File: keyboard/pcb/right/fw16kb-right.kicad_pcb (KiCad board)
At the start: 2 copper layers, 0 parts

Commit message: keyboard right PCB: outline + 2-layer stackup, 55 footprints, mirrored placement (diodes on B.Cu); pcb-spec §9: right outer-column socket pads near the edge
Co-Authored-By: Claude Opus 5.5 (1M context) <noreply@anthropic.com>
Claude-Session: https://claude.ai/code/session_019QA2U79cSHCaAaMe6Km575
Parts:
- added C1: 10u 10V X5R, Capacitor_SMD:C_0805_2012Metric, F.Cu at (-105.0, -16.0)
- added D1: 1N4148W, Diode_SMD:D_SOD-123, B.Cu at (0.00, -29.3)
- added D10: 1N4148W, Diode_SMD:D_SOD-123, B.Cu at (-54.0, -21.3)
- added D11: 1N4148W, Diode_SMD:D_SOD-123, B.Cu at (-72.0, -17.3)
- added D12: 1N4148W, Diode_SMD:D_SOD-123, B.Cu at (-90.0, -15.3)
- added D13: 1N4148W, Diode_SMD:D_SOD-123, B.Cu at (0.00, 4.70)
- added D14: 1N4148W, Diode_SMD:D_SOD-123, B.Cu at (-18.0, 4.70)
- added D15: 1N4148W, Diode_SMD:D_SOD-123, B.Cu at (-36.0, -1.30)
- added D16: 1N4148W, Diode_SMD:D_SOD-123, B.Cu at (-54.0, -4.30)
- added D17: 1N4148W, Diode_SMD:D_SOD-123, B.Cu at (-72.0, -0.30)
- added D18: 1N4148W, Diode_SMD:D_SOD-123, B.Cu at (-90.0, 1.70)
- added D19: 1N4148W, Diode_SMD:D_SOD-123, B.Cu at (-63.0, 19.7)
- added D2: 1N4148W, Diode_SMD:D_SOD-123, B.Cu at (-18.0, -29.3)
- added D20: 1N4148W, Diode_SMD:D_SOD-123, B.Cu at (-81.6, 21.7)
- added D21: 1N4148W, Diode_SMD:D_SOD-123, B.Cu at (-99.4, 27.4)
- added D22: B5819W, Diode_SMD:D_SOD-123, F.Cu at (-105.0, -20.5)
- added D3: 1N4148W, Diode_SMD:D_SOD-123, B.Cu at (-36.0, -35.3)
- added D4: 1N4148W, Diode_SMD:D_SOD-123, B.Cu at (-54.0, -38.3)
- added D5: 1N4148W, Diode_SMD:D_SOD-123, B.Cu at (-72.0, -34.3)
- added D6: 1N4148W, Diode_SMD:D_SOD-123, B.Cu at (-90.0, -32.3)
- added D7: 1N4148W, Diode_SMD:D_SOD-123, B.Cu at (0.00, -12.3)
- added D8: 1N4148W, Diode_SMD:D_SOD-123, B.Cu at (-18.0, -12.3)
- added D9: 1N4148W, Diode_SMD:D_SOD-123, B.Cu at (-36.0, -18.3)
- added H1: M2, MountingHole:MountingHole_2.2mm_M2, F.Cu at (7.45, 199.7)
- added H2: M2, MountingHole:MountingHole_2.2mm_M2, F.Cu at (7.45, 209.6)
- added H3: M2, MountingHole:MountingHole_2.2mm_M2, F.Cu at (7.45, 219.5)
- added H4: M2, MountingHole:MountingHole_2.2mm_M2, F.Cu at (7.45, 229.4)
- added J1: HRO TYPE-C-31-M-12, Connector_USB:USB_C_Receptacle_HRO_TYPE-C-31-M-12, F.Cu at (-122.0, -14.0)
- added R1: 1k, Resistor_SMD:R_0805_2012Metric, F.Cu at (-101.5, -16.0)
- added R2: 1k, Resistor_SMD:R_0805_2012Metric, F.Cu at (-101.5, -11.0)
- added R3: 330, Resistor_SMD:R_0805_2012Metric, F.Cu at (-108.5, -11.0)
- added R4: 10k, Resistor_SMD:R_0805_2012Metric, F.Cu at (-112.0, -16.0)
- added SW1: Choc v1, fw16kb:Choc_v1_Hotswap, F.Cu at (0.00, -34.0)
- added SW10: Choc v1, fw16kb:Choc_v1_Hotswap, F.Cu at (-54.0, -26.0)
- added SW11: Choc v1, fw16kb:Choc_v1_Hotswap, F.Cu at (-72.0, -22.0)
- added SW12: Choc v1, fw16kb:Choc_v1_Hotswap, F.Cu at (-90.0, -20.0)
- added SW13: Choc v1, fw16kb:Choc_v1_Hotswap, F.Cu at (0.00, 0.00)
- added SW14: Choc v1, fw16kb:Choc_v1_Hotswap, F.Cu at (-18.0, 0.00)
- added SW15: Choc v1, fw16kb:Choc_v1_Hotswap, F.Cu at (-36.0, -6.00)
- added SW16: Choc v1, fw16kb:Choc_v1_Hotswap, F.Cu at (-54.0, -9.00)
- added SW17: Choc v1, fw16kb:Choc_v1_Hotswap, F.Cu at (-72.0, -5.00)
- added SW18: Choc v1, fw16kb:Choc_v1_Hotswap, F.Cu at (-90.0, -3.00)
- added SW19: Choc v1, fw16kb:Choc_v1_Hotswap, F.Cu at (-63.0, 15.0)
- added SW2: Choc v1, fw16kb:Choc_v1_Hotswap, F.Cu at (-18.0, -34.0)
- added SW20: Choc v1, fw16kb:Choc_v1_Hotswap, F.Cu at (-82.6, 17.1)
- added SW21: Choc v1, fw16kb:Choc_v1_Hotswap, F.Cu at (-101.3, 23.1)
- added SW3: Choc v1, fw16kb:Choc_v1_Hotswap, F.Cu at (-36.0, -40.0)
- added SW4: Choc v1, fw16kb:Choc_v1_Hotswap, F.Cu at (-54.0, -43.0)
- added SW5: Choc v1, fw16kb:Choc_v1_Hotswap, F.Cu at (-72.0, -39.0)
- added SW6: Choc v1, fw16kb:Choc_v1_Hotswap, F.Cu at (-90.0, -37.0)
- added SW7: Choc v1, fw16kb:Choc_v1_Hotswap, F.Cu at (0.00, -17.0)
- added SW8: Choc v1, fw16kb:Choc_v1_Hotswap, F.Cu at (-18.0, -17.0)
- added SW9: Choc v1, fw16kb:Choc_v1_Hotswap, F.Cu at (-36.0, -23.0)
- added U1: RP2040-Zero, fw16kb:RP2040-Zero_Castellated, F.Cu at (-110.0, -34.8)
- added U2: USBLC6-2SC6, Package_TO_SOT_SMD:SOT-23-6, F.Cu at (-112.0, -11.0)
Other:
- board outline added: 132 x 88.1 mm

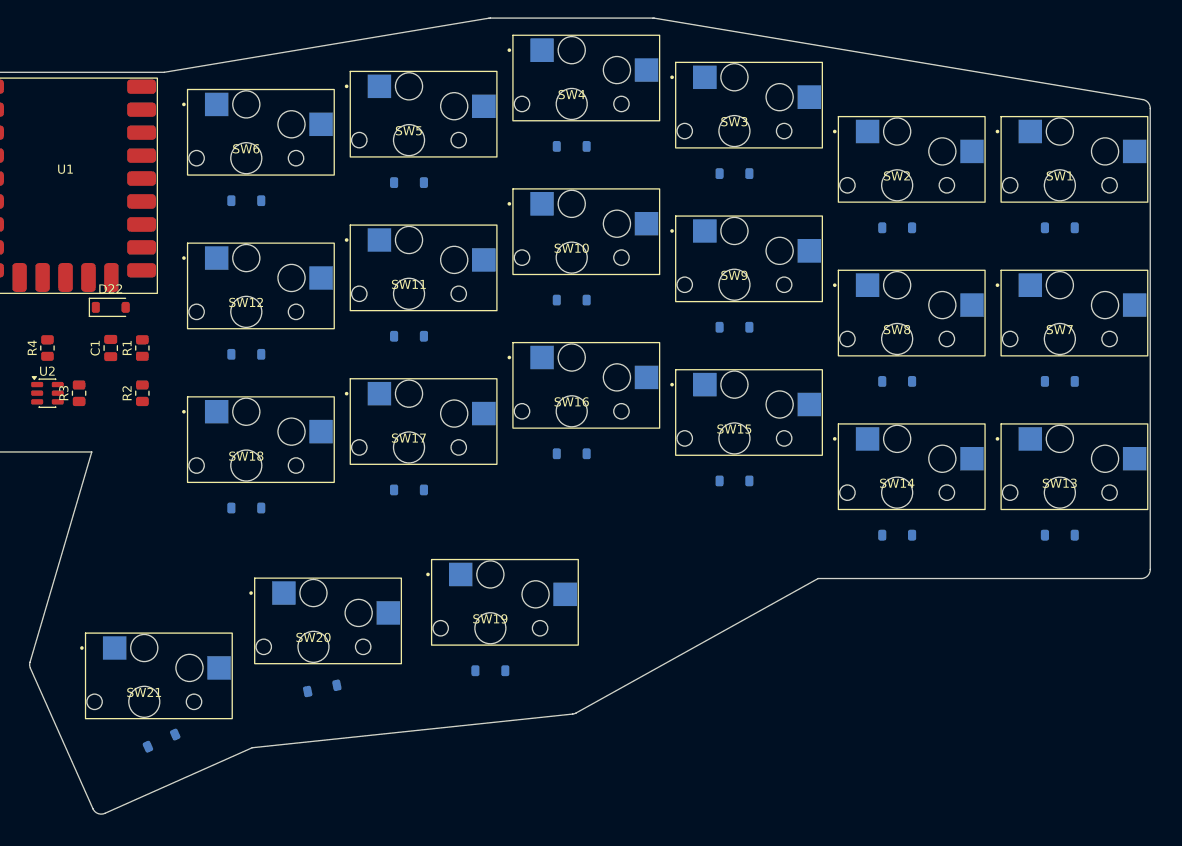
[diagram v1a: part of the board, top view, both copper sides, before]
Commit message: keyboard right PCB: widened outline imported, Choc footprints refreshed, SW20/SW21 at +12/+24; DRC: only J1 shield 0.25 mm from edge (>= JLC 0.2)
Co-Authored-By: Claude Opus 5.5 (1M context) <noreply@anthropic.com>
Claude-Session: https://claude.ai/code/session_019QA2U79cSHCaAaMe6Km575
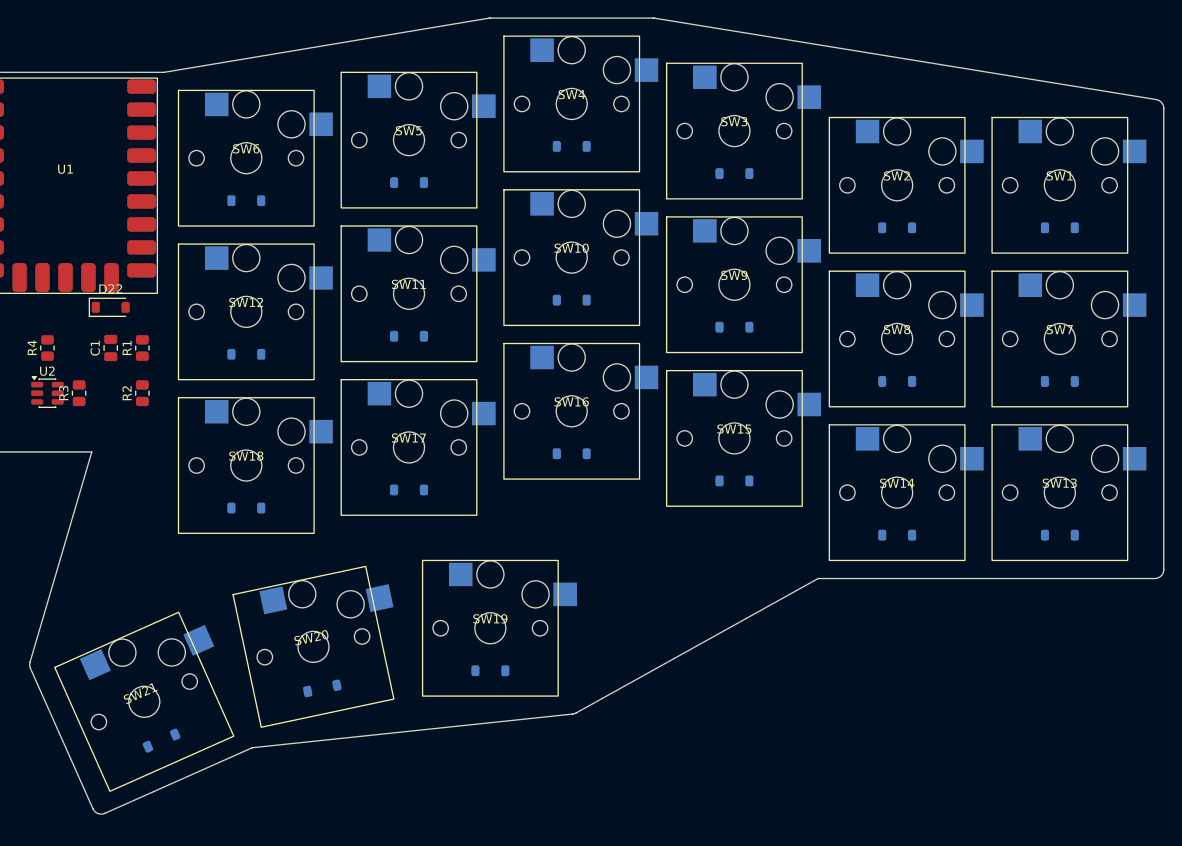
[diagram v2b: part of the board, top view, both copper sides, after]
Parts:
- turned SW20 to 12 degrees
- turned SW21 to 24 degrees
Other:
- board size 132 x 88.1 mm -> 133.5 x 88.1 mm

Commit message: keyboard right PCB: M2 holes H1-H4 (H1 shifted to -23.5 to clear SW3's unmirrored socket); chat log
Co-Authored-By: Claude Opus 5.5 (1M context) <noreply@anthropic.com>
Claude-Session: https://claude.ai/code/session_019QA2U79cSHCaAaMe6Km575
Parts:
- moved H4 259.6 mm to (-102.0, -6.00)
- moved H1 247.2 mm to (-23.5, -45.5)
- moved H3 226.1 mm to (-62.5, 4.50)
- moved H2 207.5 mm to (-30.0, 5.50)
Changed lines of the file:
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@@
 		(capping no)
 		(filling no)
-		(zone_defaults)
 		(pcbplotparams
 			(layerselection 0x00000000_00000000_55555555_5755f5ff)
@@
 	(footprint "MountingHole:MountingHole_2.2mm_M2"
 		(layer "F.Cu")
-		(at 7.45 209.61)
+		(at -30 5.5)
 		(property "Reference" "H2"
 			(at 0 -3.15 0)
@@
 	(footprint "MountingHole:MountingHole_2.2mm_M2"
 		(layer "F.Cu")
-		(at 7.45 199.71)
+		(at -23.5 -45.5)
 		(property "Reference" "H1"
 			(at 0 -3.15 0)
@@
 	(footprint "MountingHole:MountingHole_2.2mm_M2"
 		(layer "F.Cu")
-		(at 7.45 219.51)
+		(at -62.5 4.5)
 		(property "Reference" "H3"
 			(at 0 -3.15 0)
@@
 	(footprint "MountingHole:MountingHole_2.2mm_M2"
 		(layer "F.Cu")
-		(at 7.45 229.41)
+		(at -102 -6)
 		(property "Reference" "H4"
 			(at 0 -3.15 0)
@@
 		(at -99.374 27.432 24)
 		(property "Reference" "D21"
-			(at 0 2 -156)
+			(at 0 2 204)
 			(unlocked yes)
 			(layer "B.SilkS")
@@
 		)
 		(property "Value" "1N4148W"
-			(at 0 -2.1 -156)
+			(at 0 -2.1 204)
 			(unlocked yes)
 			(layer "B.SilkS")
@@
 		)
 		(property "Datasheet" ""
-			(at 0 0 -156)
+			(at 0 0 204)
 			(layer "B.Fab")
 			(hide yes)
@@
 		)
 		(property "Description" ""
-			(at 0 0 -156)
+			(at 0 0 204)
 			(layer "B.Fab")
 			(hide yes)
@@
 		)
 		(fp_text user "${REFERENCE}"
-			(at 0 2 -156)
+			(at 0 2 204)
 			(unlocked yes)
 			(layer "B.Fab")
@@
 		(at -81.593 21.654 12)
 		(property "Reference" "D20"
-			(at 0 2 -168)
+			(at 0 2 192)
 			(unlocked yes)
 			(layer "B.SilkS")
@@
 		)
 		(property "Value" "1N4148W"
-			(at 0 -2.1 -168)
+			(at 0 -2.1 192)
 			(unlocked yes)
 			(layer "B.SilkS")
@@
 		)
 		(property "Datasheet" ""
-			(at 0 0 -168)
+			(at 0 0 192)
 			(layer "B.Fab")
 			(hide yes)
@@
 		)
 		(property "Description" ""
-			(at 0 0 -168)
+			(at 0 0 192)
 			(layer "B.Fab")
 			(hide yes)
@@
 		)
 		(fp_text user "${REFERENCE}"
-			(at 0 2 -168)
+			(at 0 2 192)
 			(unlocked yes)
 			(layer "B.Fab")
@@
 		(end -121 -46.5)
 		(stroke
-			(width 0)
+			(width 0.1)
 			(type default)
 		)
@@
 		(end -122 -45.5)
 		(stroke
-			(width 0)
+			(width 0.1)
 			(type default)
 		)
@@
 		(end -99.082762 -46.5)
 		(stroke
-			(width 0)
+			(width 0.1)
 			(type default)
 		)
@@
 		(end -122 -5.5)
 		(stroke
-			(width 0)
+			(width 0.1)
 			(type default)
 		)
@@
 		(end -107.093306 -4.5)
 		(stroke
-			(width 0)
+			(width 0.1)
 			(type default)
 		)
@@
 		(end -113.924448 18.751517)
 		(stroke
-			(width 0)
+			(width 0.1)
 			(type default)
 		)
@@
 		(end -121 -4.5)
 		(stroke
-			(width 0)
+			(width 0.1)
 			(type default)
 		)
@@
 		(end -113.878544 19.440134)
 		(stroke
-			(width 0)
+			(width 0.1)
 			(type default)
 		)
@@
 		(end -106.964021 34.970407)
 		(stroke
-			(width 0)
+			(width 0.1)
 			(type default)
 		)
@@
 		(end -63.164399 -52.486394)
 		(stroke
-			(width 0)
+			(width 0.1)
 			(type default)
 		)
@@
 		(end -105.643739 35.477216)
 		(stroke
-			(width 0)
+			(width 0.1)
 			(type default)
 		)
@@
 		(end -63 -52.5)
 		(stroke
-			(width 0)
+			(width 0.1)
 			(type default)
 		)
@@
 		(end -45 -52.5)
 		(stroke
-			(width 0)
+			(width 0.1)
 			(type default)
 		)
@@
 		(end -89.344612 28.220377)
 		(stroke
-			(width 0)
+			(width 0.1)
 			(type default)
 		)
@@
 		(end -53.895472 24.494522)
 		(stroke
-			(width 0)
+			(width 0.1)
 			(type default)
 		)
@@
 		(end -44.835601 -52.486394)
 		(stroke
-			(width 0)
+			(width 0.1)
 			(type default)
 		)
@@
 		(end -53.514357 24.374157)
 		(stroke
-			(width 0)
+			(width 0.1)
 			(type default)
 		)
@@
 		(end -26.740874 9.5)
 		(stroke
-			(width 0)
+			(width 0.1)
 			(type default)
 		)
@@
 		(end -44.835601 -52.486394)
 		(stroke
-			(width 0)
+			(width 0.1)
 			(type default)
 		)
@@
 		(end 11.5 -42.5)
 		(stroke
-			(width 0)
+			(width 0.1)
 			(type default)
 		)
@@
 		(end 10.5 9.5)
 		(stroke
-			(width 0)
+			(width 0.1)
 			(type default)
 		)
@@
 		(end 11.5 -42.5)
 		(stroke
-			(width 0)
+			(width 0.1)
 			(type default)
 		)
@@
 		)
 	)
-	(group ""
-		(members "057badf5-2948-4cbf-8f02-2eac748a542a" "10e901be-5255-4d5d-b9e6-6c1ba52c0334"
-			"503eb915-0fc0-4f12-bf46-6916765d4c28" "50f0f2a1-6049-4209-a49d-d881975413eb"
-			"5fa417c8-9914-4426-bc73-cfc9d6c88e4e" "78521747-235c-430a-ae65-81b013d10f50"
-			"8839553d-e547-4101-81a4-6b1b67626a41" "8f042069-8cc1-4411-ac28-13a00fddf50d"
-			"a341a40d-0416-4dab-b1f3-9104f2ba6959" "bebba52e-0de0-40fc-b416-17f780be2070"
-			"c9b32d58-f247-4291-bbd3-1254b45bf741" "ca0b60c1-1f7a-4b00-91ae-2a7f23662b0c"
-			"d156fe42-ed1d-40d0-a9cc-d3cc766f3740" "d20a8fc7-4f4b-4797-b2b2-7b1d33cceabb"
-			"ddc8deef-8ccb-4f59-b405-141fc45781e9" "e50570aa-cd63-4174-a636-5db31becc3a5"
-			"e7d85c3c-30ec-43f0-aaac-c61be4dd7b1d" "ed674142-c0d6-48f3-837e-b3bcbfad0888"
-			"f03b4f12-162d-40a3-ab92-c6afee9fd9de" "f3b4a9b9-71d5-4708-947e-3585b6e0091f"
-			"f7574db6-7728-4ec2-9e49-866fe855dbcf" "f8298bae-12da-4cac-9853-f328257c81c7"
-		)
-	)

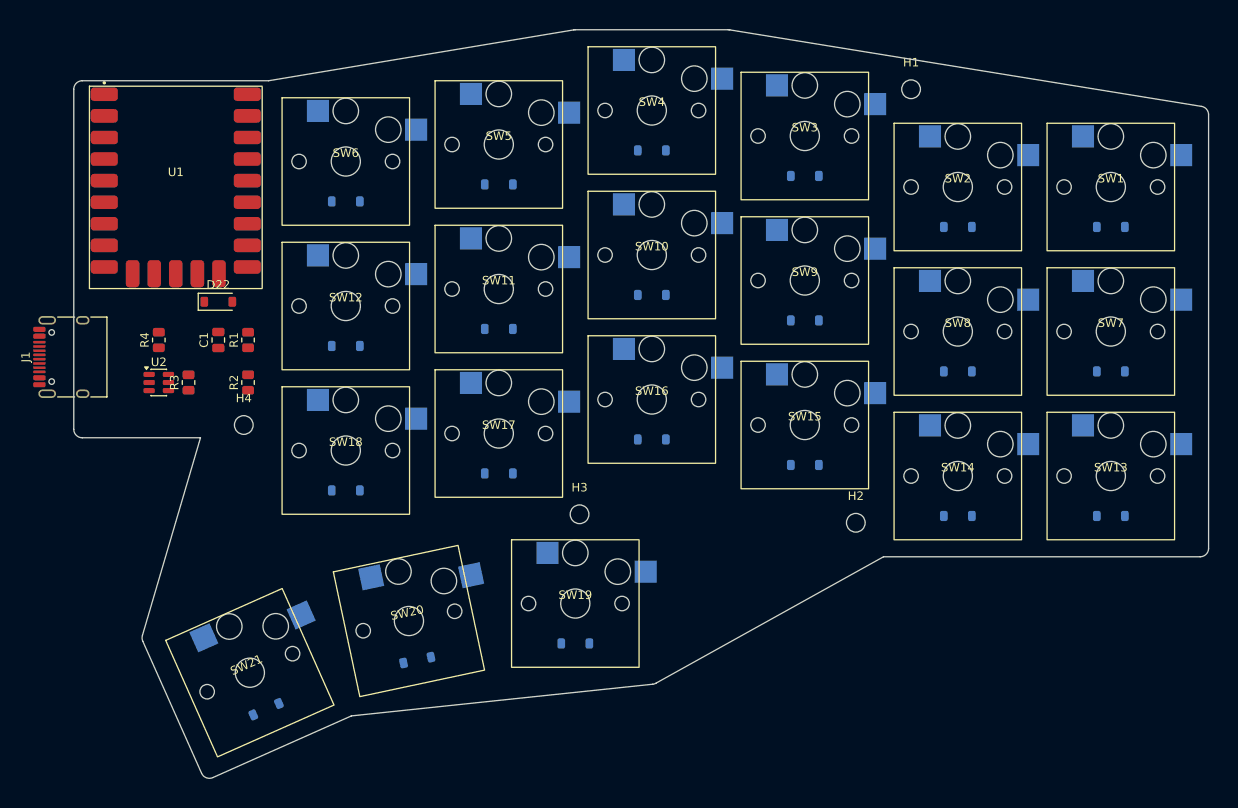
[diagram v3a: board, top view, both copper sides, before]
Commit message: keyboard right PCB: J1 turned mouth-out (1 mm overhang), link parts 2.5 mm inward; routed (freerouting + SW3-D3 by hand), GND pours both layers; DRC 0 errors
Co-Authored-By: Claude Opus 5.5 (1M context) <noreply@anthropic.com>
Claude-Session: https://claude.ai/code/session_019QA2U79cSHCaAaMe6Km575
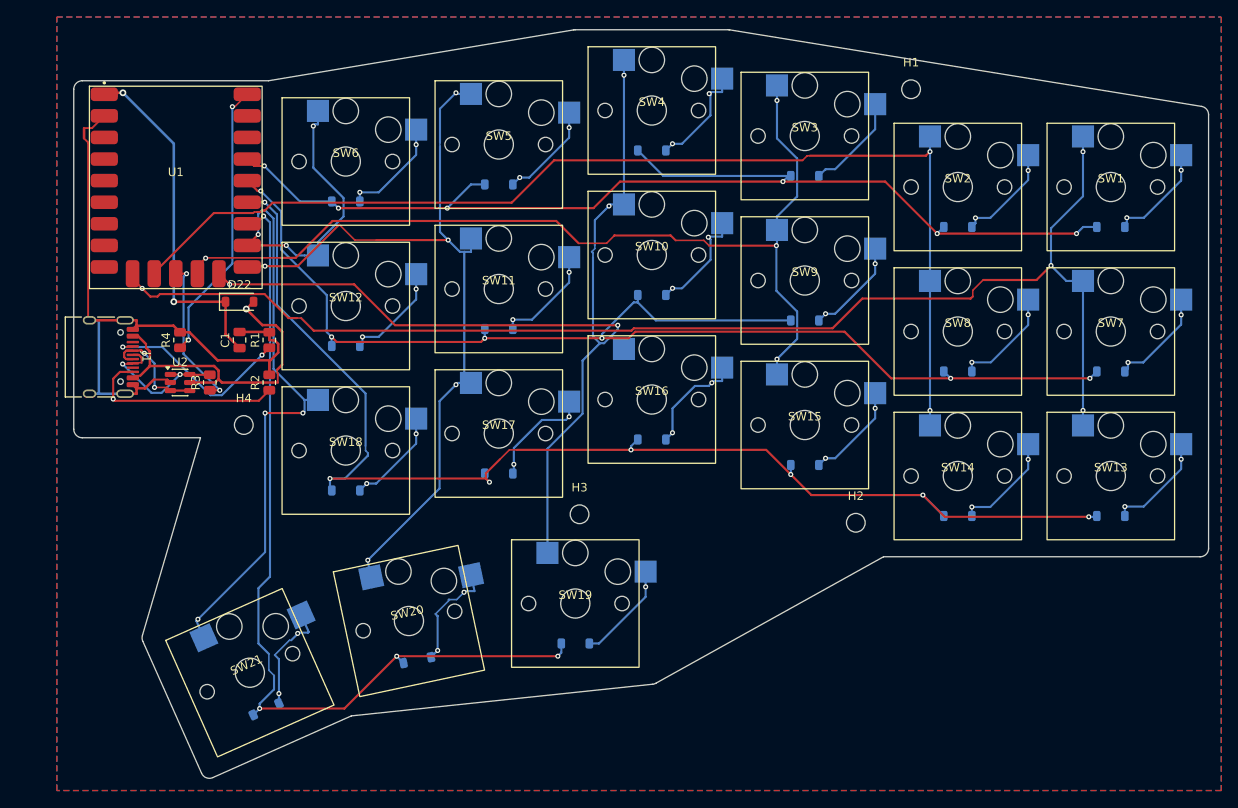
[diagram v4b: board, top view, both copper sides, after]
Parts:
- moved J1 2.90 mm to (-119.1, -14.0), turned to -90 degrees
- moved C1 2.50 mm to (-102.5, -16.0)
- moved D22 2.50 mm to (-102.5, -20.5)
- moved R1 2.50 mm to (-99.0, -16.0)
- moved R2 2.50 mm to (-99.0, -11.0)
- moved R3 2.50 mm to (-106.0, -11.0)
- moved R4 2.50 mm to (-109.5, -16.0)
- moved U2 2.50 mm to (-109.5, -11.0)
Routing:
- net /C0: track 0.00 -> 153.3 mm, vias 0 -> 4
- net /R2: track 0.00 -> 147.2 mm, vias 0 -> 7
- net /R1: track 0.00 -> 145.4 mm, vias 0 -> 6
- net /R0: track 0.00 -> 133.6 mm, vias 0 -> 6
- net /C1: track 0.00 -> 131.3 mm, vias 0 -> 2
- net /C3: track 0.00 -> 118.3 mm, vias 0 -> 4
- net /C2: track 0.00 -> 111.2 mm, vias 0 -> 4
- net /R3: track 0.00 -> 104.0 mm, vias 0 -> 4
- net /C5: track 0.00 -> 96.0 mm, vias 0 -> 6
- net /C4: track 0.00 -> 95.9 mm, vias 0 -> 5
- net /GND: track 0.00 -> 80.9 mm
- net /+5V: track 0.00 -> 41.5 mm, vias 0 -> 2
- net /LINK_VBUS: track 0.00 -> 40.1 mm, vias 0 -> 1
- net /HAND: track 0.00 -> 33.3 mm, vias 0 -> 2
- net /LINK_CC2: track 0.00 -> 24.0 mm, vias 0 -> 1
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- added copper zone on B.Cu, net /GND
- added copper zone on F.Cu, net /GND

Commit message: keyboard right PCB: single-layer vias removed (KiCad cleanup); DRC 0 errors, silk/lib-path warnings only
Co-Authored-By: Claude Opus 5.5 (1M context) <noreply@anthropic.com>
Claude-Session: https://claude.ai/code/session_019QA2U79cSHCaAaMe6Km575
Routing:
- net Net-(D9-A): vias 2 -> 0
- net Net-(D8-A): vias 2 -> 0
- net Net-(D7-A): vias 2 -> 0
- net Net-(D6-A): vias 2 -> 0
- net Net-(D5-A): vias 2 -> 0
- net Net-(D4-A): vias 2 -> 0
- net Net-(D21-A): vias 2 -> 0
- net Net-(D20-A): vias 2 -> 0
- net Net-(D2-A): vias 2 -> 0
- net Net-(D19-A): vias 1 -> 0
- net Net-(D18-A): vias 2 -> 0
- net Net-(D17-A): vias 2 -> 0
- net Net-(D16-A): vias 2 -> 0
- net Net-(D15-A): vias 2 -> 0
- net Net-(D14-A): vias 2 -> 0
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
